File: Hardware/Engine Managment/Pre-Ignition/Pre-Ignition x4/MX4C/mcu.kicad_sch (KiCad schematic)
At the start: 1 part

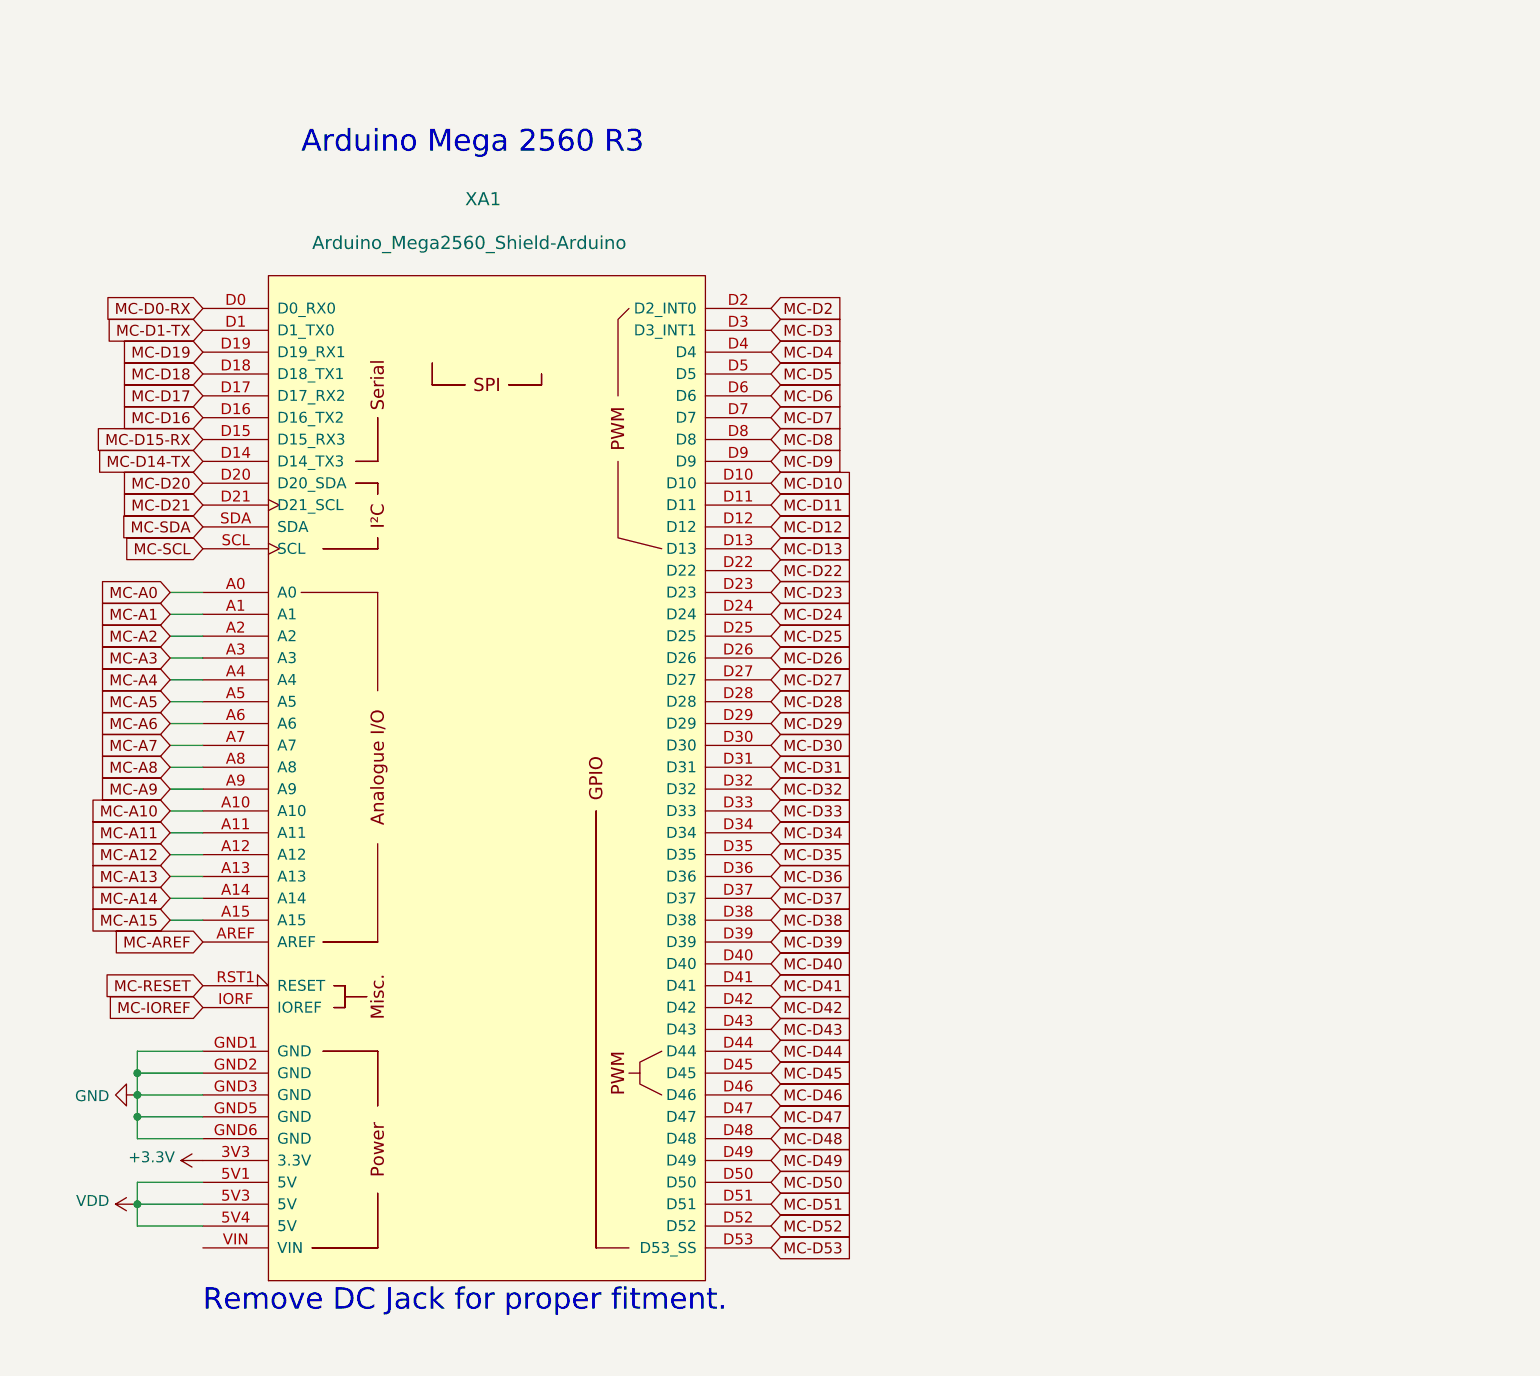
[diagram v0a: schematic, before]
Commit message: Upload correct initial upload files
Initial upload files were accidently taken from an alpha folder. 5v pins on main connector had no voltage. To fix the issue on any manufactured boards remove C8 and C9. Then short the pins of the removed capacitors.
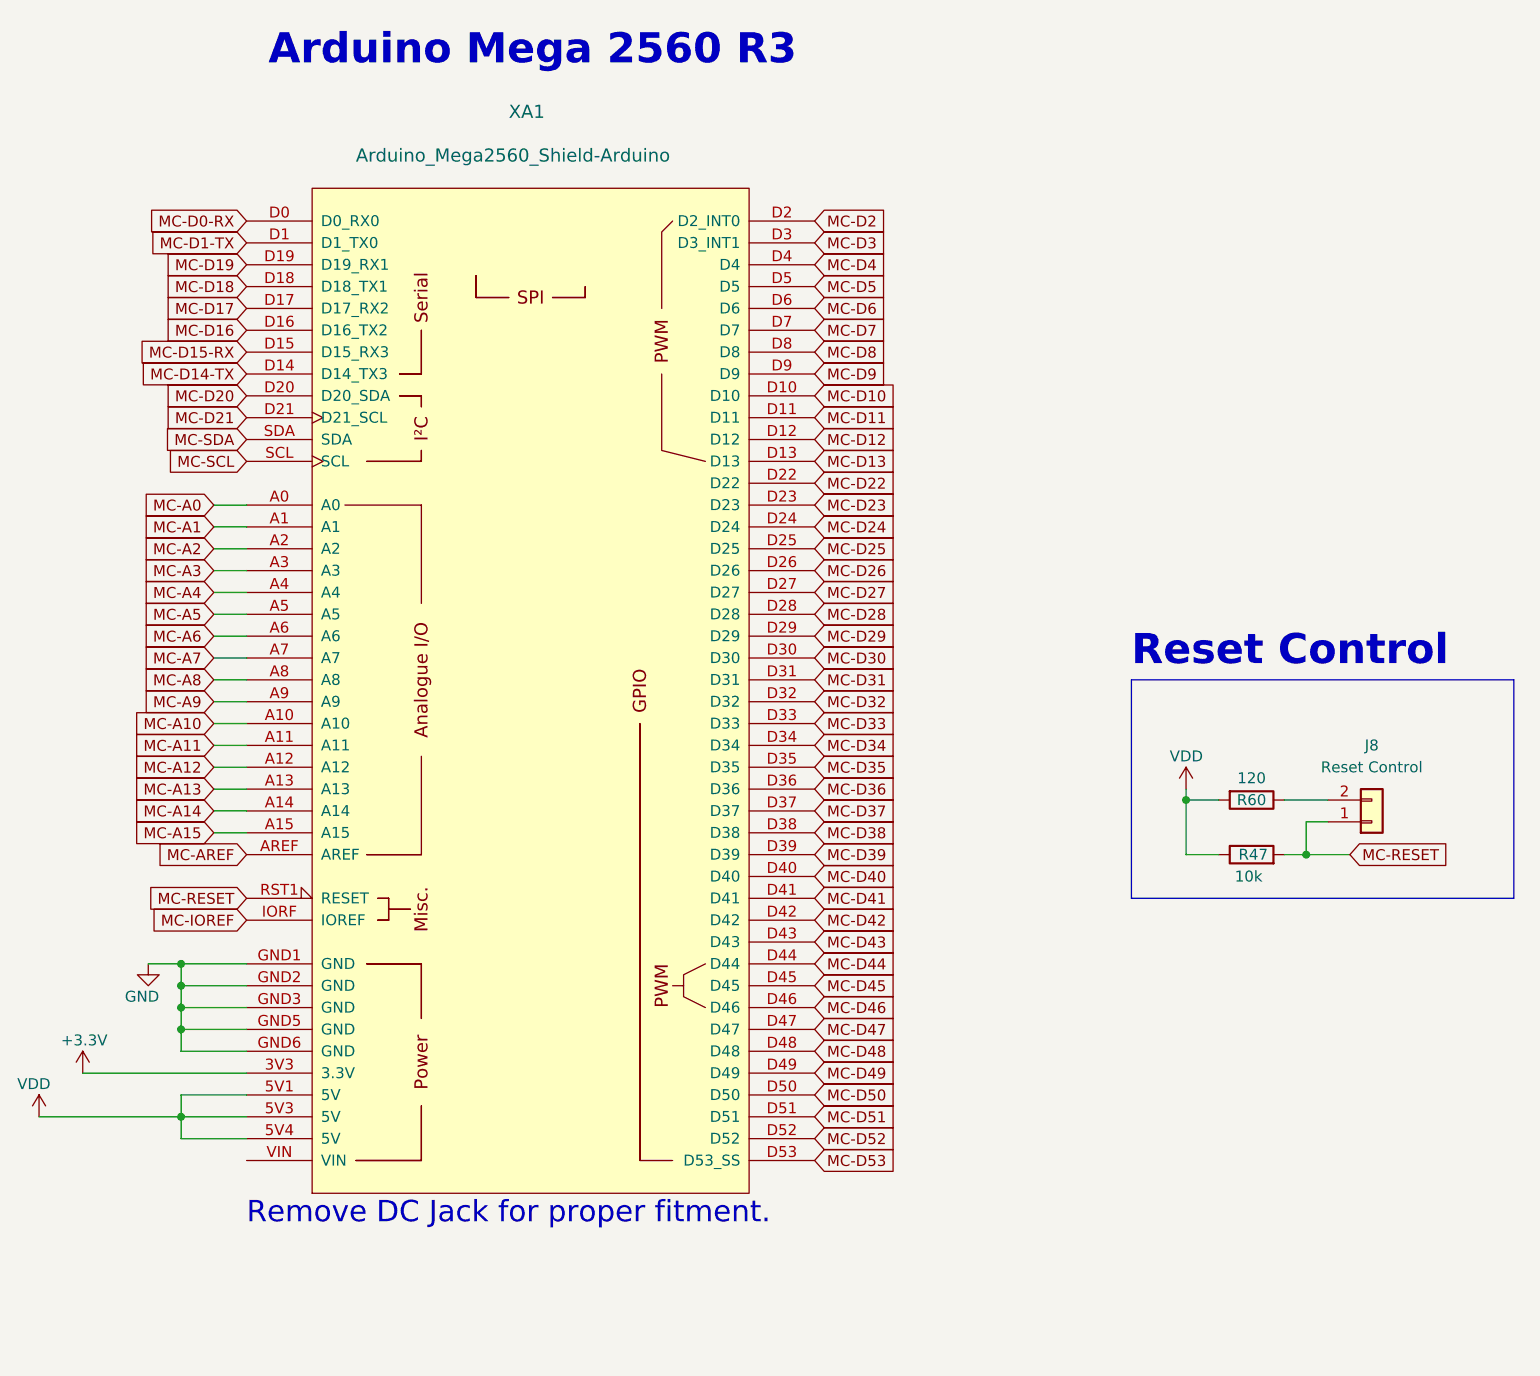
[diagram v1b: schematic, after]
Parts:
- added J8: Reset Control, Detonation:1x02-Proto, symbol Connector_Generic:Conn_01x02
- added R47: 10k, Resistor_SMD:R_0603_1608Metric, symbol Device:R
- added R60: 120, Resistor_SMD:R_0402_1005Metric, symbol Device:R
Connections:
- net MC-RESET: now also J8.1 (Pin_1), R47.2
- net VDD: now also R47.1, R60.2
- new net: J8.2 (Pin_2), R60.1
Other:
- note added: "Reset Control"
- moved on the sheet: XA1

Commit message: Structure Update
MX2 - RevB Upload
MX4B-2 - KiCad Version update (no changes)
MX4C - Organized Schematic, Minor layout change
Engine Simulator 8 Channel - Organized Schematic (no changes)
PMAP-M - Map Sensor Breakout for MX4C
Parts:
- renumbered R60 to R50
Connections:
- net VDD renamed +5V
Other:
- note added: "MCU"
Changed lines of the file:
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@@
   (title_block
     (title "Pre-Ignition X4")
-    (date "2023-05-11")
-    (rev "C2")
+    (date "2023-06-15")
+    (rev "C")
     (company "DetonationEMS")
     (comment 1 "detonationems.com")
@@
     (stroke (width 0) (type default))
   )
-  (wire (pts (xy 173.99 109.22) (xy 173.99 107.95))
+  (wire (pts (xy 173.99 109.22) (xy 173.99 105.41))
     (stroke (width 0) (type default))
   )
@@
   )
   (text "Reset Control" (at 167.64 93.98 0)
+    (effects (font (size 3.5 3.5) (thickness 0.7) bold) (justify left bottom))
+  )
+  (text "MCU" (at 179.07 172.72 0)
     (effects (font (size 3.5 3.5) (thickness 0.7) bold) (justify left bottom))
   )
@@
     )
   )
+  (symbol (lib_id "power:+5V") (at 40.64 146.05 0) (unit 1)
+    (in_bom yes) (on_board yes) (dnp no) (fields_autoplaced)
+    (property "Reference" "#PWR019" (at 40.64 149.86 0)
+      (effects (font (size 1.27 1.27)) hide)
+    )
+    (property "Value" "+5V" (at 40.64 142.24 0)
+      (effects (font (size 1.27 1.27)))
+    )
+    (property "Footprint" "" (at 40.64 146.05 0)
+      (effects (font (size 1.27 1.27)) hide)
+    )
+    (property "Datasheet" "" (at 40.64 146.05 0)
+      (effects (font (size 1.27 1.27)) hide)
+    )
+    (pin "1")
+    (instances
+      (project "Pre_Ignition"
+        (path "/929a9b03-e99e-4b88-8e16-759f8c6b59a5/00000000-0000-0000-0000-000060bdae25"
+          (reference "#PWR019") (unit 1)
+        )
+        (path "/929a9b03-e99e-4b88-8e16-759f8c6b59a5/651424fd-2282-475b-821e-32691fc06f26"
+          (reference "#PWR020") (unit 1)
+        )
+      )
+    )
+  )
   (symbol (lib_id "power:GND") (at 53.34 128.27 0) (unit 1)
     (in_bom yes) (on_board yes) (dnp no)
@@
   (symbol (lib_id "Device:R") (at 181.61 109.22 270) (unit 1)
     (in_bom yes) (on_board yes) (dnp no)
-    (property "Reference" "R60" (at 181.61 109.22 90)
+    (property "Reference" "R50" (at 181.61 109.22 90)
       (effects (font (size 1.27 1.27)))
     )
@@
       (project "Pre_Ignition"
         (path "/929a9b03-e99e-4b88-8e16-759f8c6b59a5/651424fd-2282-475b-821e-32691fc06f26"
-          (reference "R60") (unit 1)
+          (reference "R50") (unit 1)
         )
       )
@@
     )
   )
-  (symbol (lib_id "power:VDD") (at 173.99 107.95 0) (unit 1)
-    (in_bom yes) (on_board yes) (dnp no)
-    (property "Reference" "#PWR0109" (at 173.99 111.76 0)
-      (effects (font (size 1.27 1.27)) hide)
-    )
-    (property "Value" "VDD" (at 172.085 104.14 0)
-      (effects (font (size 1.27 1.27)) (justify left))
-    )
-    (property "Footprint" "" (at 173.99 107.95 0)
-      (effects (font (size 1.27 1.27)) hide)
-    )
-    (property "Datasheet" "" (at 173.99 107.95 0)
+  (symbol (lib_id "power:+5V") (at 173.99 105.41 0) (unit 1)
+    (in_bom yes) (on_board yes) (dnp no) (fields_autoplaced)
+    (property "Reference" "#PWR019" (at 173.99 109.22 0)
+      (effects (font (size 1.27 1.27)) hide)
+    )
+    (property "Value" "+5V" (at 173.99 101.6 0)
+      (effects (font (size 1.27 1.27)))
+    )
+    (property "Footprint" "" (at 173.99 105.41 0)
+      (effects (font (size 1.27 1.27)) hide)
+    )
+    (property "Datasheet" "" (at 173.99 105.41 0)
       (effects (font (size 1.27 1.27)) hide)
     )
@@
     (instances
       (project "Pre_Ignition"
+        (path "/929a9b03-e99e-4b88-8e16-759f8c6b59a5/00000000-0000-0000-0000-000060bdae25"
+          (reference "#PWR019") (unit 1)
+        )
         (path "/929a9b03-e99e-4b88-8e16-759f8c6b59a5/651424fd-2282-475b-821e-32691fc06f26"
-          (reference "#PWR0109") (unit 1)
+          (reference "#PWR019") (unit 1)
         )
       )
@@
         )
       )
-    )
-  )
-  (symbol (lib_id "power:VDD") (at 40.64 146.05 0) (unit 1)
-    (in_bom yes) (on_board yes) (dnp no)
-    (property "Reference" "#PWR0130" (at 40.64 149.86 0)
-      (effects (font (size 1.27 1.27)) hide)
-    )
-    (property "Value" "VDD" (at 38.1 142.24 0)
-      (effects (font (size 1.27 1.27)) (justify left))
-    )
-    (property "Footprint" "" (at 40.64 146.05 0)
-      (effects (font (size 1.27 1.27)) hide)
-    )
-    (property "Datasheet" "" (at 40.64 146.05 0)
-      (effects (font (size 1.27 1.27)) hide)
-    )
-    (pin "1")
-    (instances
-      (project "Pre_Ignition"
-        (path "/929a9b03-e99e-4b88-8e16-759f8c6b59a5/651424fd-2282-475b-821e-32691fc06f26"
-          (reference "#PWR0130") (unit 1)
-        )
-      )
